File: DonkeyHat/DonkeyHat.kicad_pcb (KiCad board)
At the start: 2 copper layers, 65 x 56.1 mm, 16 parts, among them J1 GPIO, J2 Encoder 2, J3 Encoder 1, U1 ProMicro

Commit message: v03
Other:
- board text added: "+ S1 S2"
- board text added: "-"
- board text added: "Donkeyhat V0.2"
- board text added: "I2C - + SCL SDA"
- board text added: "In1"
- board text added: "In2"
- board text added: "In3"
- board text added: "Steer"
- board text added: "Throt"
- board text removed: "- + S1 S2"
- board text removed: "1"
- board text removed: "2"
- board text removed: "Donkeyhat V0.1"
- board text removed: "St"
- board text removed: "Thr"
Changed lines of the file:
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@@
 		(tags "Through hole pin header THT 1x04 2.54mm single row")
 		(property "Reference" "J2"
-			(at 0 -2.33 270)
+			(at 0 -2.33 -90)
 			(layer "F.SilkS")
 			(hide yes)
@@
 		)
 		(property "Value" "Encoder 2"
-			(at 0 9.949999 270)
+			(at 0 9.949999 -90)
 			(layer "F.Fab")
 			(hide yes)
@@
 			(at 0 7.605 90)
 			(layer "F.SilkS")
+			(hide yes)
 			(effects
 				(font
@@
 		(tags "Through hole pin header THT 1x03 2.54mm single row")
 		(property "Reference" "In2"
-			(at 0 7.605001 90)
+			(at 3.106 -20.032999 90)
 			(layer "F.SilkS")
+			(hide yes)
 			(effects
 				(font
@@
 		(tags "Through hole pin header THT 1x04 2.54mm single row")
 		(property "Reference" "J3"
-			(at 0 -2.33 270)
+			(at 0 -2.33 -90)
 			(layer "F.SilkS")
 			(hide yes)
@@
 		)
 		(property "Value" "Encoder 1"
-			(at 0 9.949999 270)
+			(at 0 9.949999 -90)
 			(layer "F.Fab")
 			(hide yes)
@@
 			(at -0.127 7.605 90)
 			(layer "F.SilkS")
+			(hide yes)
 			(effects
 				(font
@@
 		(tags "Through hole pin header THT 1x04 2.54mm single row")
 		(property "Reference" "I2C"
-			(at 0 -2.33 180)
+			(at -2.681 -1.469 90)
 			(layer "F.SilkS")
+			(hide yes)
 			(effects
 				(font
@@
 		(layer "Edge.Cuts")
 	)
-	(gr_text "2"
-		(at 106.1 93.8 90)
+	(gr_text "I2C -  +  SCL SDA"
+		(at 114.9 84.4 90)
+		(layer "F.SilkS")
+		(effects
+			(font
+				(size 0.8 0.8)
+				(thickness 0.2)
+				(bold yes)
+			)
+			(justify left bottom)
+		)
+	)
+	(gr_text "Encoders"
+		(at 106.7 92.8 -90)
 		(layer "F.SilkS")
 		(effects
@@
 		)
 	)
-	(gr_text "Thr"
-		(at 101.397 86.792 90)
+	(gr_text "   +  S1 S2"
+		(at 109.1 92.4 0)
 		(layer "F.SilkS")
 		(effects
 			(font
-				(size 1 1)
-				(thickness 0.2)
-				(bold yes)
+				(size 0.9 0.9)
+				(thickness 0.15)
 			)
 			(justify left bottom)
 		)
 	)
-	(gr_text "- + SCL SDA"
-		(at 115.4 82.7 90)
+	(gr_text "S  +  -"
+		(at 108.763 91.11 180)
 		(layer "F.SilkS")
 		(effects
 			(font
 				(size 1 1)
-				(thickness 0.2)
+				(thickness 0.25)
 				(bold yes)
 			)
@@
 		)
 	)
-	(gr_text "St"
-		(at 101.397 90.475 90)
+	(gr_text "Steer"
+		(at 100.3 83.5 270)
 		(layer "F.SilkS")
 		(effects
 			(font
 				(size 1 1)
-				(thickness 0.2)
-				(bold yes)
+				(thickness 0.15)
 			)
 			(justify left bottom)
 		)
 	)
-	(gr_text "Encoders"
-		(at 107.4 99.7 90)
+	(gr_text "Throt"
+		(at 100.3 88.1 270)
 		(layer "F.SilkS")
 		(effects
@@
 		)
 	)
-	(gr_text "-  +  S1 S2"
-		(at 108.7 92.4 0)
+	(gr_text "- 5V +"
+		(at 115.367 90.5 90)
 		(layer "F.SilkS")
 		(effects
 			(font
-				(size 0.9 0.9)
+				(size 0.8 0.8)
 				(thickness 0.15)
 			)
@@
 		)
 	)
-	(gr_text "S  +  -"
-		(at 108.763 91.11 180)
+	(gr_text "In3"
+		(at 100.3 80 270)
 		(layer "F.SilkS")
 		(effects
 			(font
 				(size 1 1)
-				(thickness 0.2)
-				(bold yes)
+				(thickness 0.15)
 			)
 			(justify left bottom)
 		)
 	)
-	(gr_text "1"
-		(at 106.1 99.9 90)
+	(gr_text "In2"
+		(at 100.3 76.2 270)
 		(layer "F.SilkS")
 		(effects
@@
 		)
 	)
-	(gr_text "- 5V +"
-		(at 115.367 90.5 90)
+	(gr_text "Donkeyhat V0.2"
+		(at 117.7 88 90)
 		(layer "F.SilkS")
 		(effects
 			(font
-				(size 0.8 0.8)
+				(size 1 1)
 				(thickness 0.15)
 			)
@@
 		)
 	)
-	(gr_text "Donkeyhat V0.1"
-		(at 117.7 88 90)
+	(gr_text "-"
+		(at 108.5 100.1 0)
+		(layer "F.SilkS")
+		(effects
+			(font
+				(size 1 1)
+				(thickness 0.25)
+				(bold yes)
+			)
+			(justify left bottom)
+		)
+	)
+	(gr_text "In1"
+		(at 100.4 72.5 -90)
 		(layer "F.SilkS")
 		(effects

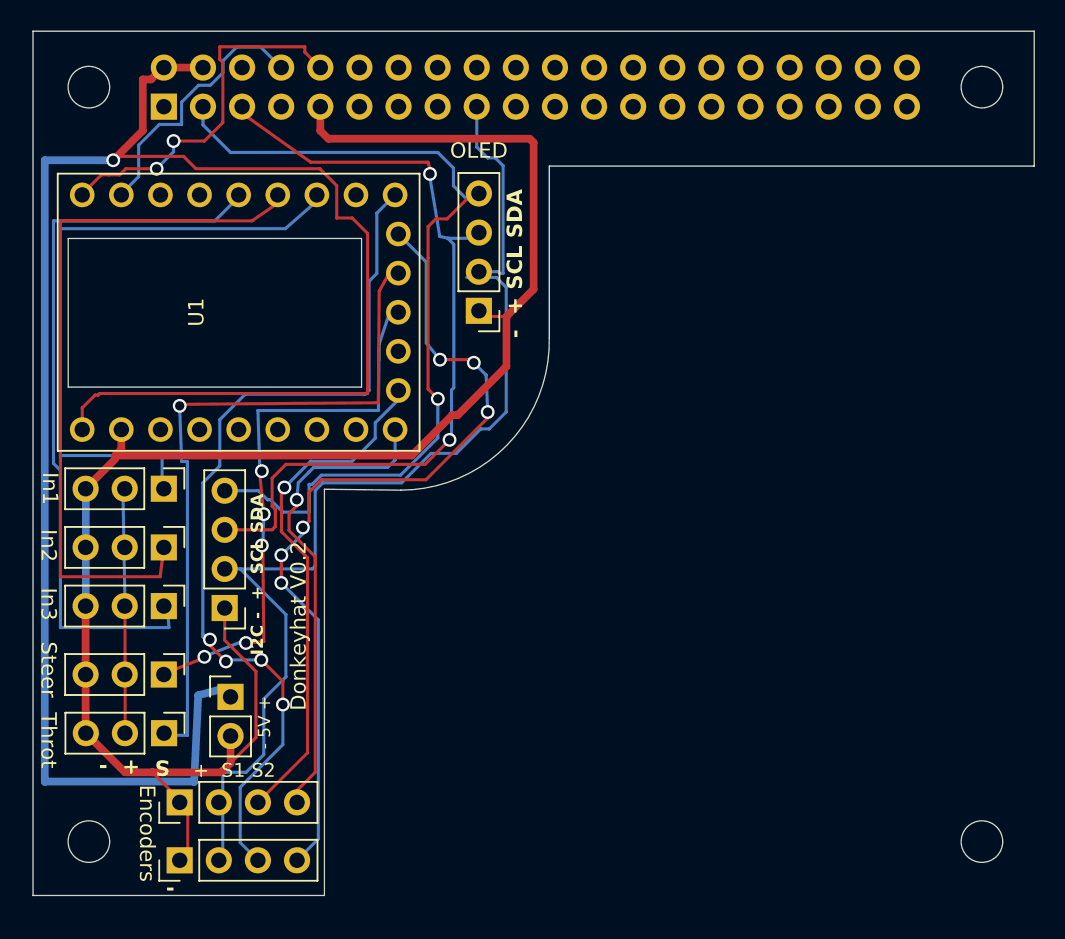
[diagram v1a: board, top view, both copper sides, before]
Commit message: catellated pins
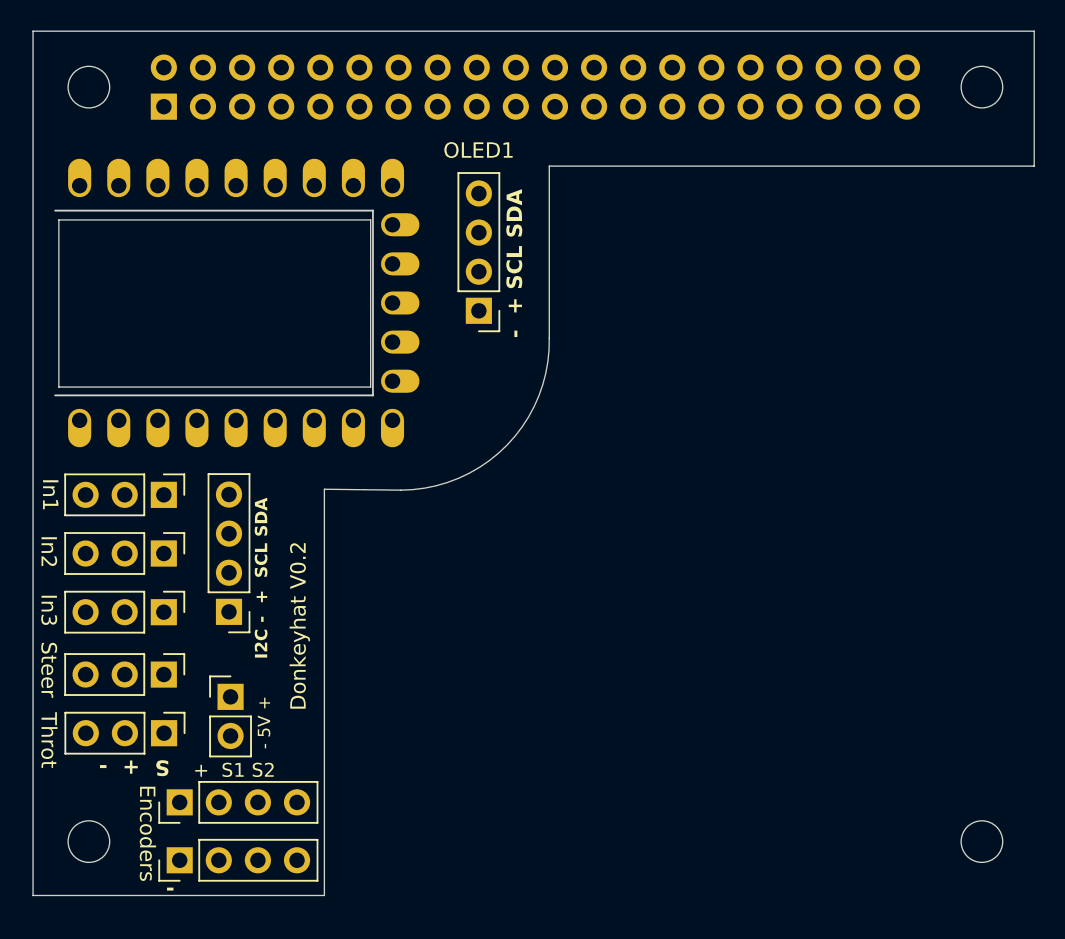
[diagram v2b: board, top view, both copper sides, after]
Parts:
- U1: footprint RP2040-Zero:RP2040-Zero-bigholes -> mcu:rp2040-zero-tht
- moved U1 15.3 mm to (113.1, 61.5)
- moved In1 0.40 mm to (108.4, 81.6)
- moved In2 0.40 mm to (108.4, 77.8)
- moved In3 0.40 mm to (108.4, 74.0)
- moved I2C1 0.38 mm to (112.6, 81.6)
- renumbered I2C to I2C1, OLED to OLED1
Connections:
- U1 pad 21: unconnected-(U1-VCC-Pad21) -> GND
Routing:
- net GND: track 105.9 -> 0.06 mm
- net +3V3: track 72.9 -> 0.36 mm
- net Net-(J2-Pin_3): track 59.2 -> 0.00 mm, vias 4 -> 0
- net Net-(J2-Pin_4): track 56.5 -> 0.00 mm, vias 6 -> 0
- net +5V: track 56.2 -> 0.00 mm, vias 1 -> 0
- net /GPIO2/SDA1: track 55.7 -> 0.00 mm, vias 1 -> 0
- net Net-(J3-Pin_3): track 33.9 -> 0.00 mm, vias 1 -> 0
- net /GPIO3/SCL1: track 33.8 -> 0.00 mm, vias 2 -> 0
- net Net-(J3-Pin_4): track 31.2 -> 0.77 mm, vias 1 -> 0
- net /GPIO15/RXD0: track 24.1 -> 0.00 mm, vias 2 -> 0
- net /GPIO14/TXD0: track 17.6 -> 0.00 mm
- net Net-(In1-Pin_1): track 10.9 -> 0.00 mm
- net Net-(Thr1-Pin_1): vias 5 -> 0
- net Net-(St1-Pin_1): vias 1 -> 0
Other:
- outline, holes or cut-outs redrawn
